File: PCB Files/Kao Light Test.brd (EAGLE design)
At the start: 68.6 x 53.3 mm, 12 parts, among them Q1 MMBT3904-TP

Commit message: feat: updates PCB
Adds changes from Issue #9
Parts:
- removed BT1, BT2, BT3: BHX1-1025-SM, BHX1-1025-SM:BAT_BHX1-1025-SM
- removed Q1: MMBT3904-TP, MMBT3904-TP:SOT-23_MCC
- added ANALOG: (no value), SparkFun-Connectors:JST-2-SMD
- added CN1: (no value), adafruit:JST-PH-2-THM
- added R10, R11, R12, R13, R14, R3, R4, R5, R6, R7, R8, R9: 1k, SparkFun-Resistors:AXIAL-0.3
- added T1: 2N2222, adafruit:TO92-EBC-OVAL
- moved LASER 56.2 mm to (62.2, 43.2), flipped to the top, turned to 270 degrees
- moved 5V_REG 40.0 mm to (61.0, 25.3), flipped to the top, turned to 180 degrees
- moved R2 34.8 mm to (46.5, 45.1), turned to 0 degrees
- moved R1 25.2 mm to (53.1, 38.9), turned to 0 degrees
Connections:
- removed net GND_2: DIGITAL-OUT.13, U$1.GND1
- removed net GND_3: BT3.-, DIGITAL-OUT.1
- removed net N$17: BT2.-, BT3.S+1, BT3.S+2
- removed net N$4: Q1.3, R2.P$1
- new net D14: ANALOG.2, DIGITAL-OUT.17
- new net VIN: U$1.VIN
- net D1: now also R14.P$2
- net D10: now also R5.P$2
- net D11: now also R4.P$2
- net D12: now also R3.P$2
- net D2: now also R13.P$2
- net D3: now also R12.P$2
- net D4: now also R11.P$2
- net D5: now also R10.P$2
- net D6: now also R9.P$2
- net D7: now also R8.P$2
- net D8: now also R7.P$2
- net D9: now also R6.P$2
- net GND_1: now also ANALOG.1, CN1.2, DIGITAL-OUT.13, R10.P$1, R11.P$1, R12.P$1, R13.P$1, R14.P$1, R3.P$1, R4.P$1, R5.P$1, R6.P$1, R7.P$1, R8.P$1, R9.P$1, T1.E, U$1.GND1; no longer Q1.2
- net N$1: now also CN1.1; no longer BT1.S+1, BT1.S+2, U$1.VIN
- net N$2: now also R1.P$2, T1.B; no longer BT1.-, BT2.S+1, BT2.S+2
- net N$3: now also R2.P$1, T1.C; no longer Q1.1, R1.P$2
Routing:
- net GND_1: track 38.5 -> 203.2 mm
- net N$1: track 74.2 -> 25.7 mm, vias 1 -> 0
- net N$2: track 58.7 -> 13.2 mm
- net GND_2: track 45.1 -> 0.00 mm
- net D5: track 57.3 -> 96.4 mm, vias 0 -> 1
- net D14: track 0.00 -> 37.7 mm
- net N$17: track 35.1 -> 0.00 mm
- net D9: track 36.7 -> 67.1 mm
- net D10: track 31.9 -> 54.4 mm
- net GND_3: track 20.1 -> 0.00 mm
- net D4: track 65.2 -> 81.3 mm
- net D8: track 47.2 -> 62.9 mm
- net D12: track 26.7 -> 41.5 mm
- net D2: track 74.4 -> 88.9 mm
- net D6: track 87.0 -> 75.0 mm
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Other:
- board text added: "Battery"
- board text added: "Laser"

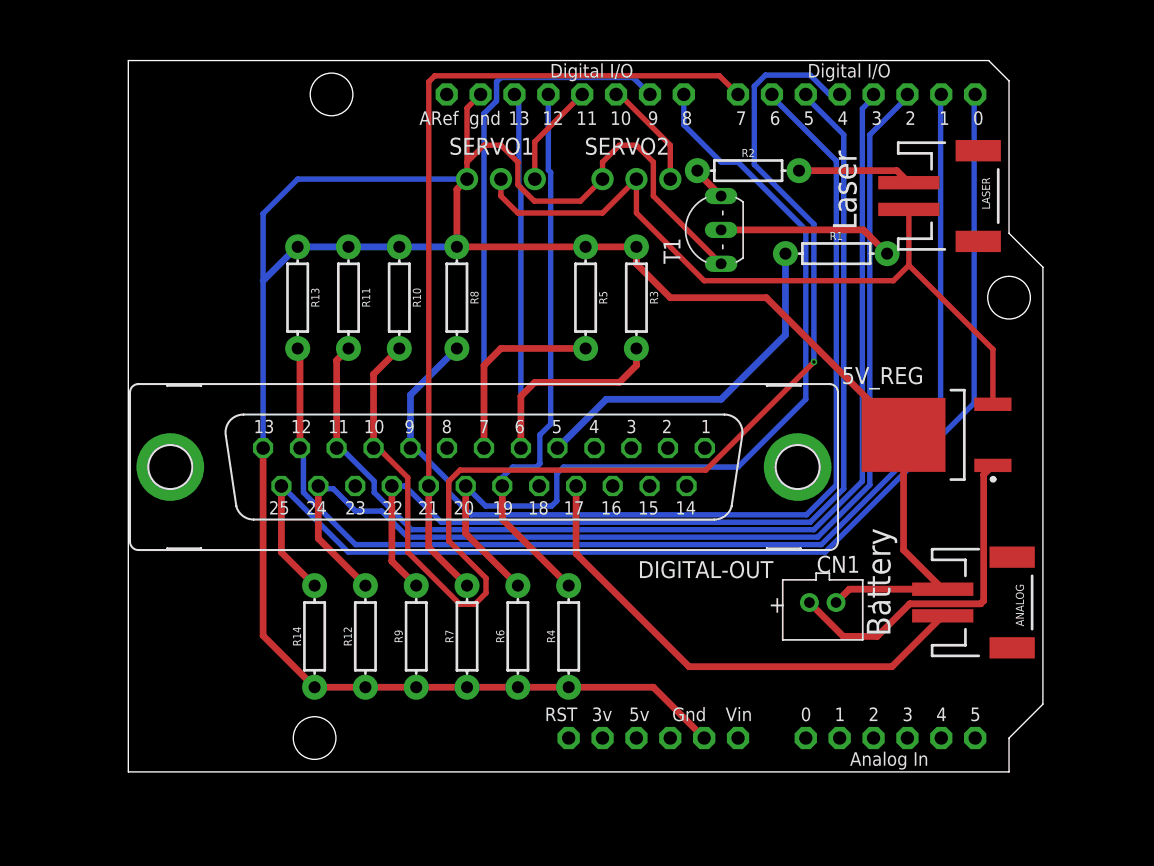
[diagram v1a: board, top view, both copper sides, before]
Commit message: feat: Improves the look of the PCB
Improves the naming and clenliness of the PCB
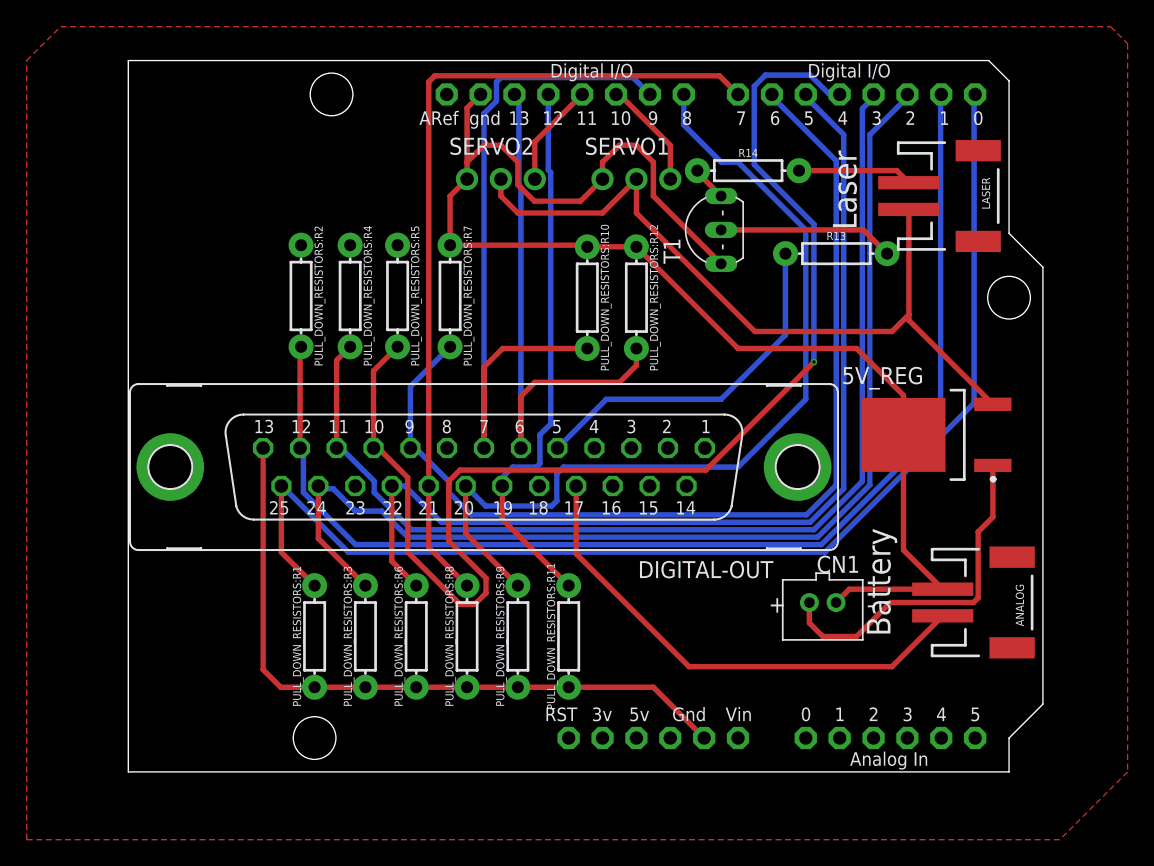
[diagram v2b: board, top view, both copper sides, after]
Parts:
- removed R1: 10k, SparkFun-Resistors:AXIAL-0.3
- removed R10, R11, R5, R8: 1k, SparkFun-Resistors:AXIAL-0.3
- removed R2: 220, SparkFun-Resistors:AXIAL-0.3
- added PULL_DOWN_RESISTORS:R1, PULL_DOWN_RESISTORS:R10, PULL_DOWN_RESISTORS:R2, PULL_DOWN_RESISTORS:R4, PULL_DOWN_RESISTORS:R5, PULL_DOWN_RESISTORS:R7: 1k, SparkFun-Resistors:AXIAL-0.3
- R13: value 1k -> 10k
- R14: value 1k -> 220
- moved R14 47.7 mm to (46.5, 45.1), turned to 0 degrees
- moved R13 40.5 mm to (53.1, 38.9), turned to 0 degrees
- moved SERVO1 10.2 mm to (38.1, 44.5)
- moved SERVO2 10.2 mm to (27.9, 44.5)
- renumbered R12 to PULL_DOWN_RESISTORS:R3, R3 to PULL_DOWN_RESISTORS:R12, R4 to PULL_DOWN_RESISTORS:R11, R6 to PULL_DOWN_RESISTORS:R9, R7 to PULL_DOWN_RESISTORS:R8, R9 to PULL_DOWN_RESISTORS:R6
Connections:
- net N$1 renamed BAT+
- net N$7 renamed 5VOUT
- removed net N$8: SERVO1.3, U$1.D11
- removed net N$9: SERVO2.3, U$1.D10
- new net PAN: SERVO1.3, U$1.D10
- new net TILT: SERVO2.3, U$1.D11
- net D1: now also PULL_DOWN_RESISTORS:R1.P$2; no longer R14.P$2
- net D10: now also PULL_DOWN_RESISTORS:R10.P$2; no longer R5.P$2
- net D13: now also R13.P$1; no longer R1.P$1
- net D2: now also PULL_DOWN_RESISTORS:R2.P$2; no longer R13.P$2
- net D4: now also PULL_DOWN_RESISTORS:R4.P$2; no longer R11.P$2
- net D5: now also PULL_DOWN_RESISTORS:R5.P$2; no longer R10.P$2
- net D7: now also PULL_DOWN_RESISTORS:R7.P$2; no longer R8.P$2
- net GND_1: now also PULL_DOWN_RESISTORS:R1.P$1, PULL_DOWN_RESISTORS:R10.P$1, PULL_DOWN_RESISTORS:R2.P$1, PULL_DOWN_RESISTORS:R4.P$1, PULL_DOWN_RESISTORS:R5.P$1, PULL_DOWN_RESISTORS:R7.P$1; no longer R10.P$1, R11.P$1, R13.P$1, R14.P$1, R5.P$1, R8.P$1
- net N$2: now also R13.P$2; no longer R1.P$2
- net N$3: now also R14.P$1; no longer R2.P$1
- net N$6: now also R14.P$2; no longer R2.P$2
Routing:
- net GND_1: track 203.2 -> 156.8 mm
- net PAN: track 0.00 -> 8.18 mm
- net N$9: track 8.18 -> 0.00 mm
- net TILT: track 0.00 -> 7.82 mm
- net N$8: track 7.82 -> 0.00 mm
- net 5VOUT: track 55.8 -> 57.4 mm
- net BAT+: track 25.7 -> 26.2 mm
- added copper zone on layer 1, net GND_1
